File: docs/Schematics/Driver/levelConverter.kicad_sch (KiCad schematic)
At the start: 0 parts

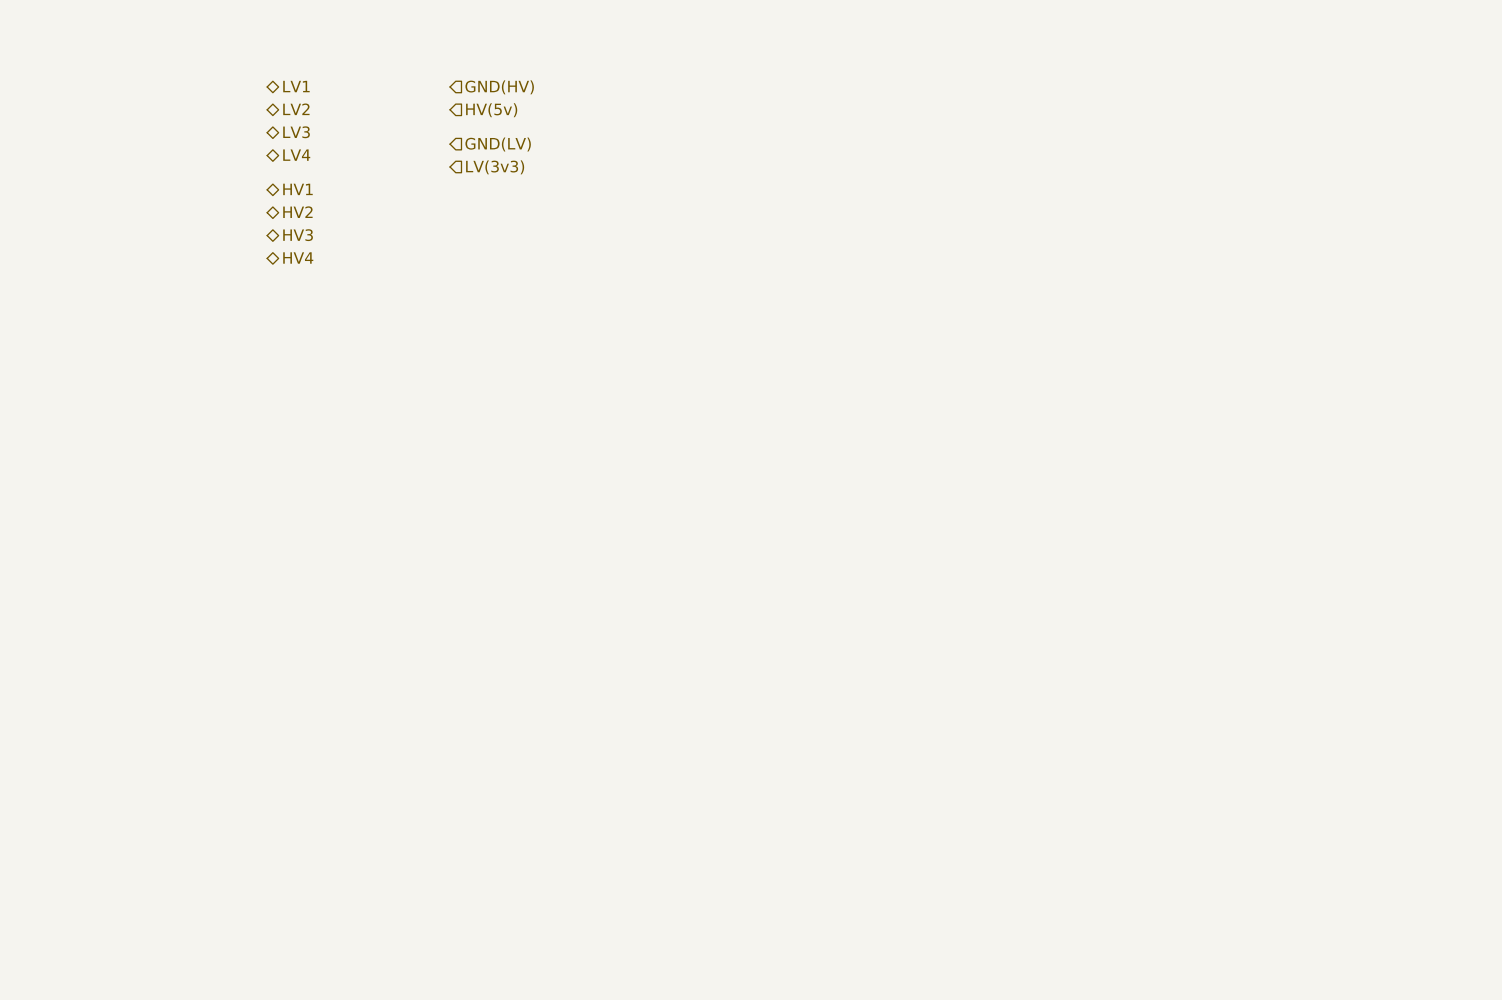
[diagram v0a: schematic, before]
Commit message: First scematic design for the card
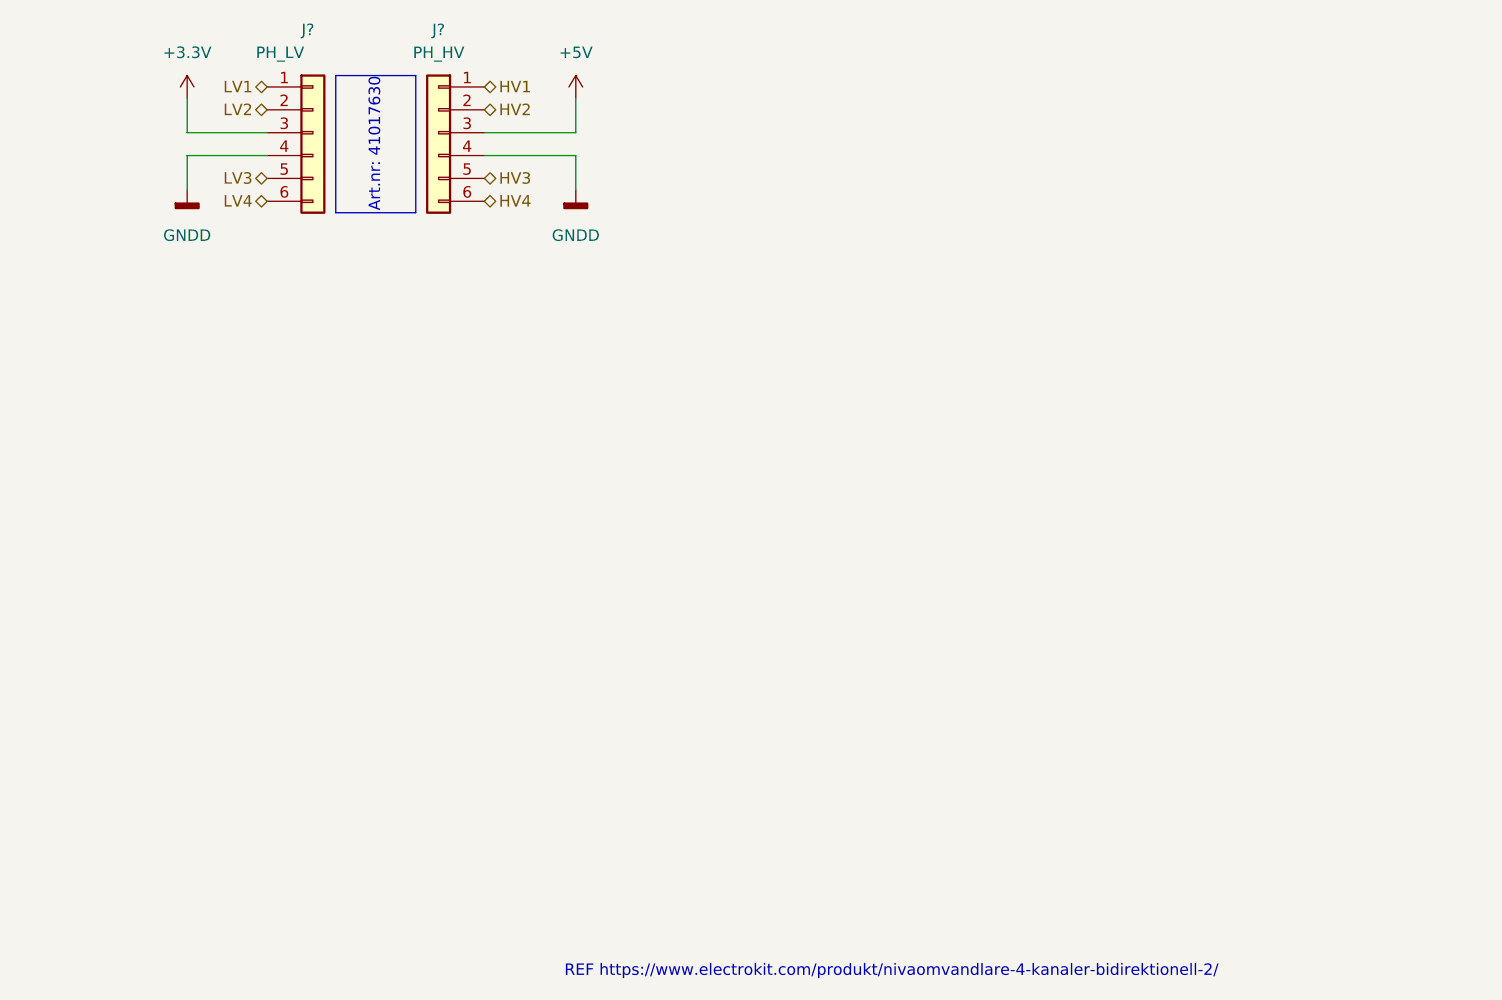
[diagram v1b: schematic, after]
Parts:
- added J?: PH_LV, symbol Connector_Generic:Conn_01x06
- added J?: PH_HV, symbol Connector_Generic:Conn_01x06
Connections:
- net HV1: now also J?.1 (Pin_1)
- net HV2: now also J?.2 (Pin_2)
- net HV3: now also J?.5 (Pin_5)
- net HV4: now also J?.6 (Pin_6)
- net LV1: now also J?.1 (Pin_1)
- net LV2: now also J?.2 (Pin_2)
- net LV3: now also J?.5 (Pin_5)
- net LV4: now also J?.6 (Pin_6)
- new net +3.3V: J?.3 (Pin_3)
- new net +5V: J?.3 (Pin_3)
- new net GNDD: J?.4 (Pin_4), J?.4 (Pin_4)
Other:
- note added: "Art.nr: 41017630"
- note added: "REF https://www.electrokit.com/produkt/nivaomvandlare-4-kanaler-bidirektionell-2/"
- company: (none) -> HiQ
- title: (none) -> Arty Z7 IO expander card
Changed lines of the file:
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@@
 (kicad_sch (version 20211123) (generator eeschema)
   (paper "A4")
-  (hierarchical_label "LV4" (shape bidirectional) (at 144.78 77.47 0)
+  (title_block
+    (title "Arty Z7 IO expander card")
+    (date "2022-12-24")
+    (rev "0.1")
+    (company "HiQ")
+  )
+  (wire (pts (xy 135.89 77.47) (xy 135.89 81.28))
+    (stroke (width 0) (type default) (color 0 0 0 0))
+  )
+  (polyline (pts (xy 152.4 68.58) (xy 152.4 83.82))
+    (stroke (width 0) (type default) (color 0 0 0 0))
+  )
+  (wire (pts (xy 135.89 71.12) (xy 135.89 74.93))
+    (stroke (width 0) (type default) (color 0 0 0 0))
+  )
+  (wire (pts (xy 168.91 74.93) (xy 179.07 74.93))
+    (stroke (width 0) (type default) (color 0 0 0 0))
+  )
+  (wire (pts (xy 135.89 74.93) (xy 144.78 74.93))
+    (stroke (width 0) (type default) (color 0 0 0 0))
+  )
+  (polyline (pts (xy 161.29 68.58) (xy 161.29 83.82))
+    (stroke (width 0) (type default) (color 0 0 0 0))
+  )
+  (polyline (pts (xy 161.29 83.82) (xy 152.4 83.82))
+    (stroke (width 0) (type default) (color 0 0 0 0))
+  )
+  (polyline (pts (xy 152.4 68.58) (xy 161.29 68.58))
+    (stroke (width 0) (type default) (color 0 0 0 0))
+  )
+  (wire (pts (xy 168.91 77.47) (xy 179.07 77.47))
+    (stroke (width 0) (type default) (color 0 0 0 0))
+  )
+  (wire (pts (xy 179.07 77.47) (xy 179.07 81.28))
+    (stroke (width 0) (type default) (color 0 0 0 0))
+  )
+  (wire (pts (xy 144.78 77.47) (xy 135.89 77.47))
+    (stroke (width 0) (type default) (color 0 0 0 0))
+  )
+  (wire (pts (xy 179.07 74.93) (xy 179.07 71.12))
+    (stroke (width 0) (type default) (color 0 0 0 0))
+  )
+  (text "REF https://www.electrokit.com/produkt/nivaomvandlare-4-kanaler-bidirektionell-2/"
+    (at 177.8 168.91 0)
+    (effects (font (size 1.27 1.27)) (justify left bottom))
+  )
+  (text "Art.nr: 41017630" (at 157.48 83.82 90)
+    (effects (font (size 1.27 1.27)) (justify left bottom))
+  )
+  (hierarchical_label "LV4" (shape bidirectional) (at 144.78 82.55 180)
+    (effects (font (size 1.27 1.27)) (justify right))
+  )
+  (hierarchical_label "HV2" (shape bidirectional) (at 168.91 72.39 0)
     (effects (font (size 1.27 1.27)) (justify left))
   )
-  (hierarchical_label "HV2" (shape bidirectional) (at 144.78 83.82 0)
+  (hierarchical_label "HV1" (shape bidirectional) (at 168.91 69.85 0)
     (effects (font (size 1.27 1.27)) (justify left))
   )
-  (hierarchical_label "HV1" (shape bidirectional) (at 144.78 81.28 0)
+  (hierarchical_label "HV3" (shape bidirectional) (at 168.91 80.01 0)
     (effects (font (size 1.27 1.27)) (justify left))
   )
-  (hierarchical_label "HV3" (shape bidirectional) (at 144.78 86.36 0)
+  (hierarchical_label "HV4" (shape bidirectional) (at 168.91 82.55 0)
     (effects (font (size 1.27 1.27)) (justify left))
   )
-  (hierarchical_label "HV4" (shape bidirectional) (at 144.78 88.9 0)
-    (effects (font (size 1.27 1.27)) (justify left))
+  (hierarchical_label "LV2" (shape bidirectional) (at 144.78 72.39 180)
+    (effects (font (size 1.27 1.27)) (justify right))
   )
-  (hierarchical_label "GND(HV)" (shape input) (at 165.1 69.85 0)
-    (effects (font (size 1.27 1.27)) (justify left))
+  (hierarchical_label "LV3" (shape bidirectional) (at 144.78 80.01 180)
+    (effects (font (size 1.27 1.27)) (justify right))
   )
-  (hierarchical_label "HV(5v)" (shape input) (at 165.1 72.39 0)
-    (effects (font (size 1.27 1.27)) (justify left))
+  (hierarchical_label "LV1" (shape bidirectional) (at 144.78 69.85 180)
+    (effects (font (size 1.27 1.27)) (justify right))
   )
-  (hierarchical_label "LV2" (shape bidirectional) (at 144.78 72.39 0)
-    (effects (font (size 1.27 1.27)) (justify left))
+  (symbol (lib_id "power:+3.3V") (at 135.89 71.12 0) (unit 1)
+    (in_bom yes) (on_board yes) (fields_autoplaced)
+    (property "Reference" "#PWR?" (id 0) (at 135.89 74.93 0)
+      (effects (font (size 1.27 1.27)) hide)
+    )
+    (property "Value" "+3.3V" (id 1) (at 135.89 66.04 0))
+    (property "Footprint" "" (id 2) (at 135.89 71.12 0)
+      (effects (font (size 1.27 1.27)) hide)
+    )
+    (property "Datasheet" "" (id 3) (at 135.89 71.12 0)
+      (effects (font (size 1.27 1.27)) hide)
+    )
+    (pin "1")
   )
-  (hierarchical_label "LV(3v3)" (shape input) (at 165.1 78.74 0)
-    (effects (font (size 1.27 1.27)) (justify left))
+  (symbol (lib_id "power:+5V") (at 179.07 71.12 0) (unit 1)
+    (in_bom yes) (on_board yes) (fields_autoplaced)
+    (property "Reference" "#PWR?" (id 0) (at 179.07 74.93 0)
+      (effects (font (size 1.27 1.27)) hide)
+    )
+    (property "Value" "+5V" (id 1) (at 179.07 66.04 0))
+    (property "Footprint" "" (id 2) (at 179.07 71.12 0)
+      (effects (font (size 1.27 1.27)) hide)
+    )
+    (property "Datasheet" "" (id 3) (at 179.07 71.12 0)
+      (effects (font (size 1.27 1.27)) hide)
+    )
+    (pin "1")
   )
-  (hierarchical_label "LV3" (shape bidirectional) (at 144.78 74.93 0)
-    (effects (font (size 1.27 1.27)) (justify left))
+  (symbol (lib_id "Connector_Generic:Conn_01x06") (at 149.86 74.93 0) (unit 1)
+    (in_bom yes) (on_board yes)
+    (property "Reference" "J?" (id 0) (at 148.59 63.5 0)
+      (effects (font (size 1.27 1.27)) (justify left))
+    )
+    (property "Value" "PH_LV" (id 1) (at 143.51 66.04 0)
+      (effects (font (size 1.27 1.27)) (justify left))
+    )
+    (property "Footprint" "" (id 2) (at 149.86 74.93 0)
+      (effects (font (size 1.27 1.27)) hide)
+    )
+    (property "Datasheet" "~" (id 3) (at 149.86 74.93 0)
+      (effects (font (size 1.27 1.27)) hide)
+    )
+    (pin "1")
+    (pin "2")
+    (pin "3")
+    (pin "4")
+    (pin "5")
+    (pin "6")
   )
-  (hierarchical_label "LV1" (shape bidirectional) (at 144.78 69.85 0)
-    (effects (font (size 1.27 1.27)) (justify left))
+  (symbol (lib_id "power:GNDD") (at 135.89 81.28 0) (unit 1)
+    (in_bom yes) (on_board yes) (fields_autoplaced)
+    (property "Reference" "#PWR?" (id 0) (at 135.89 87.63 0)
+      (effects (font (size 1.27 1.27)) hide)
+    )
+    (property "Value" "GNDD" (id 1) (at 135.89 86.36 0))
+    (property "Footprint" "" (id 2) (at 135.89 81.28 0)
+      (effects (font (size 1.27 1.27)) hide)
+    )
+    (property "Datasheet" "" (id 3) (at 135.89 81.28 0)
+      (effects (font (size 1.27 1.27)) hide)
+    )
+    (pin "1")
   )
-  (hierarchical_label "GND(LV)" (shape input) (at 165.1 76.2 0)
-    (effects (font (size 1.27 1.27)) (justify left))
+  (symbol (lib_id "Connector_Generic:Conn_01x06") (at 163.83 74.93 0) (mirror y) (unit 1)
+    (in_bom yes) (on_board yes) (fields_autoplaced)
+    (property "Reference" "J?" (id 0) (at 163.83 63.5 0))
+    (property "Value" "PH_HV" (id 1) (at 163.83 66.04 0))
+    (property "Footprint" "" (id 2) (at 163.83 74.93 0)
+      (effects (font (size 1.27 1.27)) hide)
+    )
+    (property "Datasheet" "~" (id 3) (at 163.83 74.93 0)
+      (effects (font (size 1.27 1.27)) hide)
+    )
+    (pin "1")
+    (pin "2")
+    (pin "3")
+    (pin "4")
+    (pin "5")
+    (pin "6")
+  )
+  (symbol (lib_id "power:GNDD") (at 179.07 81.28 0) (unit 1)
+    (in_bom yes) (on_board yes) (fields_autoplaced)
+    (property "Reference" "#PWR?" (id 0) (at 179.07 87.63 0)
+      (effects (font (size 1.27 1.27)) hide)
+    )
+    (property "Value" "GNDD" (id 1) (at 179.07 86.36 0))
+    (property "Footprint" "" (id 2) (at 179.07 81.28 0)
+      (effects (font (size 1.27 1.27)) hide)
+    )
+    (property "Datasheet" "" (id 3) (at 179.07 81.28 0)
+      (effects (font (size 1.27 1.27)) hide)
+    )
+    (pin "1")
   )
 )
